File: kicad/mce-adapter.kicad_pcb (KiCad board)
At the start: 2 copper layers, 63.5 x 31.6 mm, 20 parts, among them J123 Conn_02x03_Odd_Even, J4 Conn_01x03_Male, SW1 SW_DIP_x03, U1 GAL16V8B

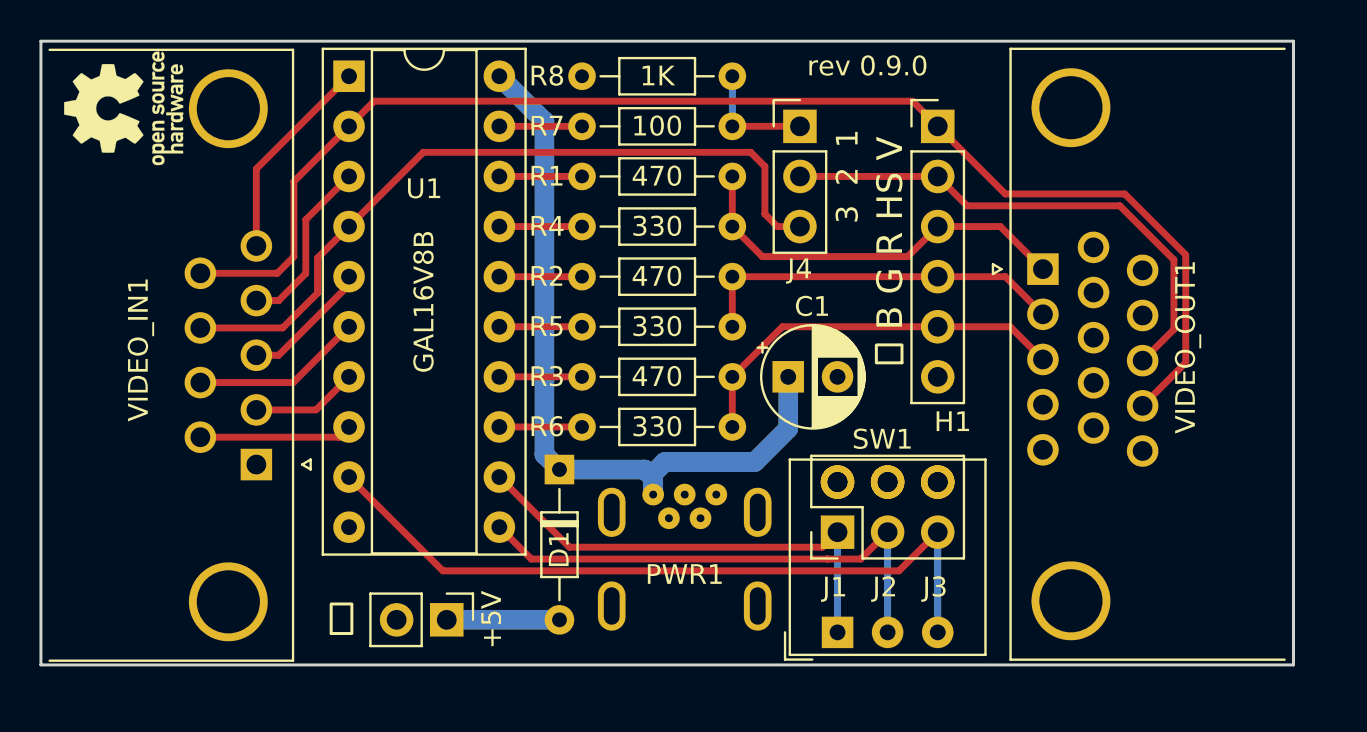
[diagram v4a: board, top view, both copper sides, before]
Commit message: Added mode auto-detection
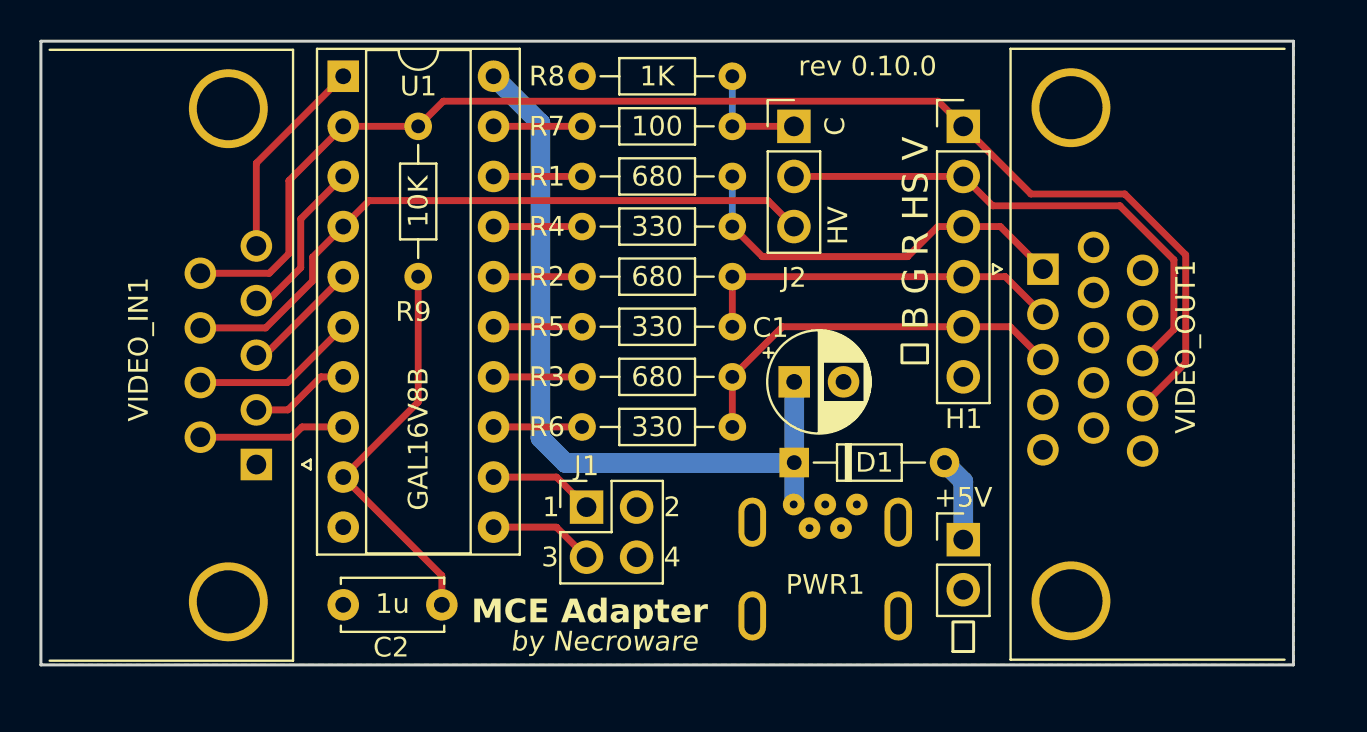
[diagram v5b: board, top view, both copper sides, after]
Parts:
- removed J123: Conn_02x03_Odd_Even, Connector_PinHeader_2.54mm:PinHeader_2x03_P2.54mm_Vertical
- removed J4: Conn_01x03_Male, Connector_PinHeader_2.54mm:PinHeader_1x03_P2.54mm_Vertical
- removed SW1: SW_DIP_x03, Button_Switch_THT:SW_DIP_SPSTx03_Slide_9.78x9.8mm_W7.62mm_P2.54mm
- added C2: 1u, Capacitor_THT:C_Disc_D5.0mm_W2.5mm_P5.00mm, F.Cu at (131.1, 115.3)
- added J1: Conn_02x02_Odd_Even, Connector_PinHeader_2.54mm:PinHeader_2x02_P2.54mm_Vertical, F.Cu at (138.4, 110.4)
- added J2: Conn_01x03_Male, Connector_PinHeader_2.54mm:PinHeader_1x03_P2.54mm_Vertical, F.Cu at (148.9, 91.1)
- added R9: 10K, Resistor_THT:R_Axial_DIN0204_L3.6mm_D1.6mm_P7.62mm_Horizontal, F.Cu at (129.9, 91.1)
- R1, R2, R3: value 470 -> 680
- REF**: moved to B.Cu
- moved REF** 59.7 mm to (169.5, 114.3), turned to -90 degrees
- moved PWR2 26.5 mm to (157.5, 112.0), turned to 0 degrees
- moved D1 11.9 mm to (148.9, 108.1), turned to 0 degrees
- moved PWR1 7.14 mm to (150.5, 110.2)
- moved H1 1.30 mm to (157.5, 91.1)
- moved C1 0.40 mm to (148.9, 104.0)
- moved U1 0.29 mm to (126.1, 88.5)
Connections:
- U1 pad 9: SW3_IN -> Net-(U1-I9)
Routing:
- net SW3_IN: track 37.7 -> 0.00 mm
- net SW2_IN: track 26.0 -> 5.35 mm
- net Net-(U1-I9): track 0.00 -> 20.3 mm
- net SW1_IN: track 24.0 -> 5.35 mm
- net H_IN: track 38.1 -> 34.0 mm
- net Net-(D1-A): track 5.71 -> 4.30 mm
- net /VCC: track 38.5 -> 39.0 mm
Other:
- board text added: "J1: off/off EGA/CGA on/on MDA white on/off MDA green off/on MDA amber"
- board text added: "J2: 1-2 C-Sync 2-3 HV-Sync"
- board text removed: "J3: color mode setting J4: sync S:1-2 H:2-3"
- board text removed: "MDA - J1:on J2:on CGA/EGA - J1:off J2:n/a HiEGA - J1:on J2:off"

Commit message: Readjusted resistor networks to get blow 0.7V
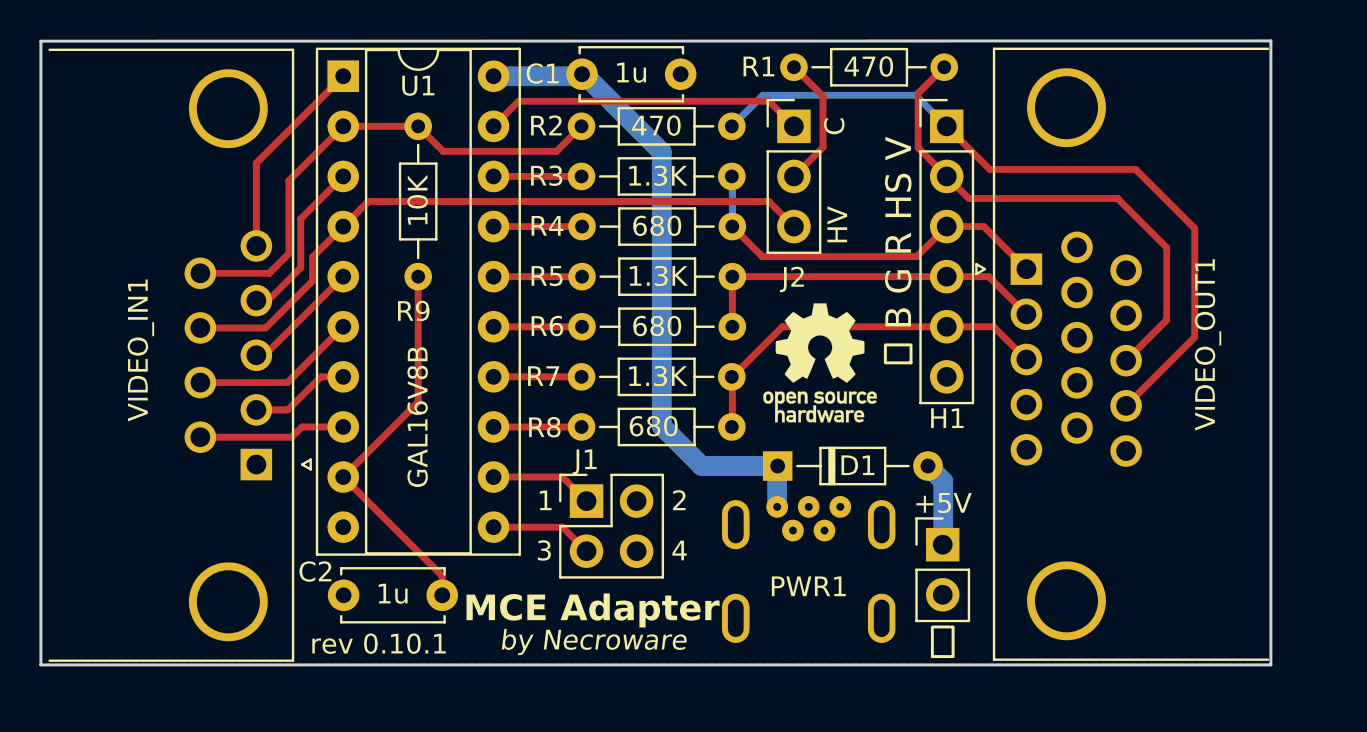
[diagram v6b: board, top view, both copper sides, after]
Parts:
- C1: value 220u -> 1u; footprint Capacitor_THT:CP_Radial_D5.0mm_P2.50mm -> Capacitor_THT:C_Disc_D5.0mm_W2.5mm_P5.00mm
- R1, R2: value 680 -> 470
- R3: value 680 -> 1.3K
- R4, R6: value 330 -> 680
- R5: value 330 -> 1.3K
- R7: value 100 -> 1.3K
- R8: value 1K -> 680
- REF**: moved to F.Cu
- moved REF** 22.3 mm to (150.2, 103.0), turned to 0 degrees
- moved C1 18.9 mm to (138.2, 88.4)
- moved R8 17.8 mm to (145.8, 106.3)
- moved R7 12.7 mm to (145.8, 103.8)
- moved R1 12.1 mm to (156.5, 88.1)
- moved R3 10.2 mm to (145.8, 93.6)
- moved R2 7.62 mm to (145.8, 91.1)
- moved R6 5.08 mm to (145.8, 101.2)
- moved R5 2.54 mm to (145.8, 98.7)
- moved PWR2 1.07 mm to (156.5, 112.3)
- moved D1 0.86 mm to (148.1, 108.3)
- moved PWR1 0.85 mm to (149.7, 110.4)
- moved H1 0.84 mm to (156.7, 91.1)
- moved VIDEO_OUT1 0.84 mm to (160.7, 98.3)
- moved C2 0.48 mm to (131.1, 114.8)
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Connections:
- net /VCC renamed Net-(D1-K)
- H1 pad 1: V_IN -> V_OUT
- J2 pad 2: H_OUT -> Net-(J2-Pin_2)
- R1 pad 1: R_OUT -> H_OUT
- R1 pad 2: Net-(U1-IO2) -> Net-(J2-Pin_2)
- R2 pad 1: G_OUT -> V_OUT
- R2 pad 2: Net-(U1-IO4) -> V_IN
- R3 pad 1: B_OUT -> R_OUT
- R3 pad 2: Net-(U1-IO6) -> Net-(U1-IO2)
- R5 pad 2: Net-(U1-IO5) -> Net-(U1-IO4)
- R6 pad 1: B_OUT -> G_OUT
- R6 pad 2: Net-(U1-IO7) -> Net-(U1-IO5)
- R7 pad 1: S_OUT -> B_OUT
- R7 pad 2: Net-(U1-IO1) -> Net-(U1-IO6)
- R8 pad 1: S_OUT -> B_OUT
- R8 pad 2: GND -> Net-(U1-IO7)
- U1 pad 19: Net-(U1-IO1) -> S_OUT
- VIDEO_OUT1 pad 14: V_IN -> V_OUT
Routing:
- net V_IN: track 67.5 -> 25.6 mm
- net V_OUT: track 0.00 -> 37.3 mm
- net S_OUT: track 5.66 -> 16.3 mm
- net Net-(J2-Pin_2): track 0.00 -> 6.76 mm
- net Net-(D1-K): track 39.0 -> 32.8 mm
- net Net-(U1-IO1): track 4.49 -> 0.00 mm
- net H_OUT: track 26.8 -> 25.9 mm
- net R_OUT: track 20.4 -> 19.6 mm
- net G_OUT: track 19.1 -> 18.2 mm
- net B_OUT: track 20.0 -> 19.2 mm
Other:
- board size 63.5 x 31.6 mm -> 62.4 x 31.6 mm
